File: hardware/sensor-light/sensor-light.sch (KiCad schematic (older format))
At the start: 15 parts, among them J1 Power IN 12V, J2 PIR Sensor 2, J3 PIR Sensor 1, J4 PROG Header, J5 Light Sensor, J6 PWM Power OUT 12V, Q1 IRLML2502, SW1 Manual ON/OFF, U1 Reg 3.3V, U2 MSP430G2553IN20

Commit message: Attempt at laying out the board
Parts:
- removed J1: Power IN 12V, Connectors:AK300-2, symbol CONN_01X02_MALE-RESCUE-sensor-light
- J6: value PWM Power OUT 12V -> Power IN/OUT 12V; footprint Connectors:AK300-2 -> Connectors:AK300-4; symbol CONN_01X02_FEMALE -> CONN_01X04_FEMALE-RESCUE-sensor-light
- R3: value 56 Ohm -> 47Ω
- R4: value 56 Ohm -> 27Ω
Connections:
- wire segments 44 -> 48
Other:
- moved on the sheet: C1, D1, D2, J2, J3, J4, J5, Q1, R3, R4, SW1, U1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

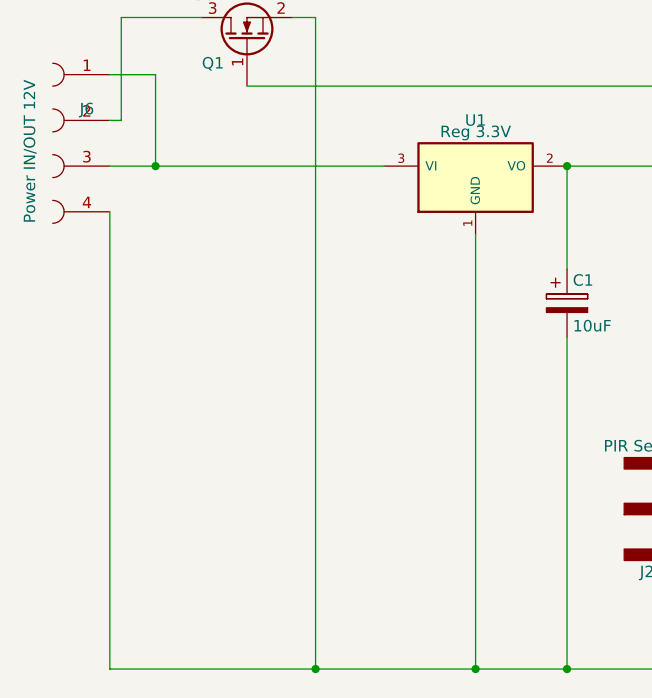
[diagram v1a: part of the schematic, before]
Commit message: add capacitor to the regulator input
Signed-off-by: Eugene Crosser <evgenii.cherkashin@profitbricks.com>
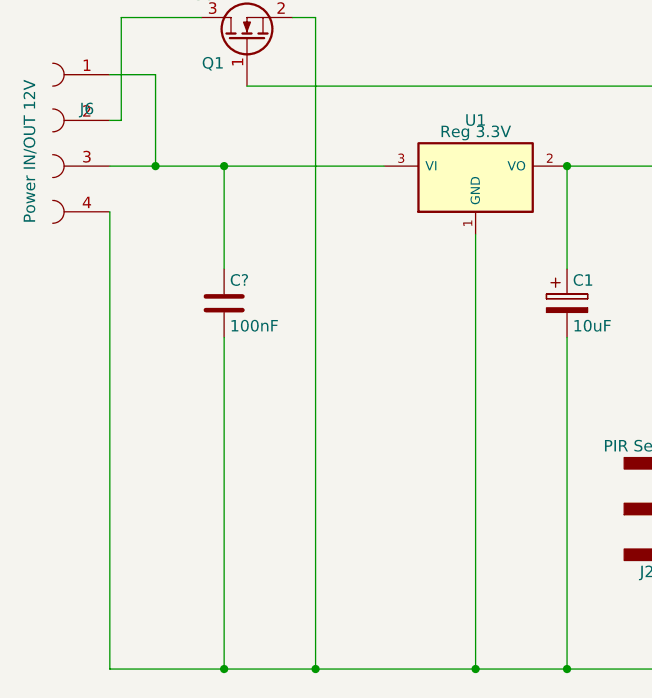
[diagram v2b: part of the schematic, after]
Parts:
- added C?: 100nF, symbol C
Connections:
- net at C1.2, D1.1 (K), D2.1 (K)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: now also C?.2
- net at J6.1, J6.3, U1.3 (VI): now also C?.1
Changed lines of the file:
@@
 Wire Wire Line
 	5300 3650 5300 4050
+$Comp
+L C C?
+U 1 1 5A8C5F51
+P 1700 3900
+F 0 "C?" H 1725 4000 50  0000 L CNN
+F 1 "100nF" H 1725 3800 50  0000 L CNN
+F 2 "" H 1738 3750 50  0000 C CNN
+F 3 "" H 1700 3900 50  0000 C CNN
+	1    1700 3900
+	1    0    0    -1
+$EndComp
+Wire Wire Line
+	1700 3750 1700 3300
+Connection ~ 1700 3300
+Wire Wire Line
+	1700 4050 1700 5500
+Connection ~ 1700 5500
 $EndSCHEMATC

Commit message: layout adjustments
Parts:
- C2: renamed from C?; footprint (none) -> Capacitors_THT:C_Rect_L7.0mm_W2.5mm_P5.00mm
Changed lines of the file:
@@
 	5300 3650 5300 4050
 $Comp
-L C C?
+L C C2
 U 1 1 5A8C5F51
 P 1700 3900
-F 0 "C?" H 1725 4000 50  0000 L CNN
+F 0 "C2" H 1725 4000 50  0000 L CNN
 F 1 "100nF" H 1725 3800 50  0000 L CNN
-F 2 "" H 1738 3750 50  0000 C CNN
+F 2 "Capacitors_THT:C_Rect_L7.0mm_W2.5mm_P5.00mm" H 1738 3750 50  0001 C CNN
 F 3 "" H 1700 3900 50  0000 C CNN
 	1    1700 3900

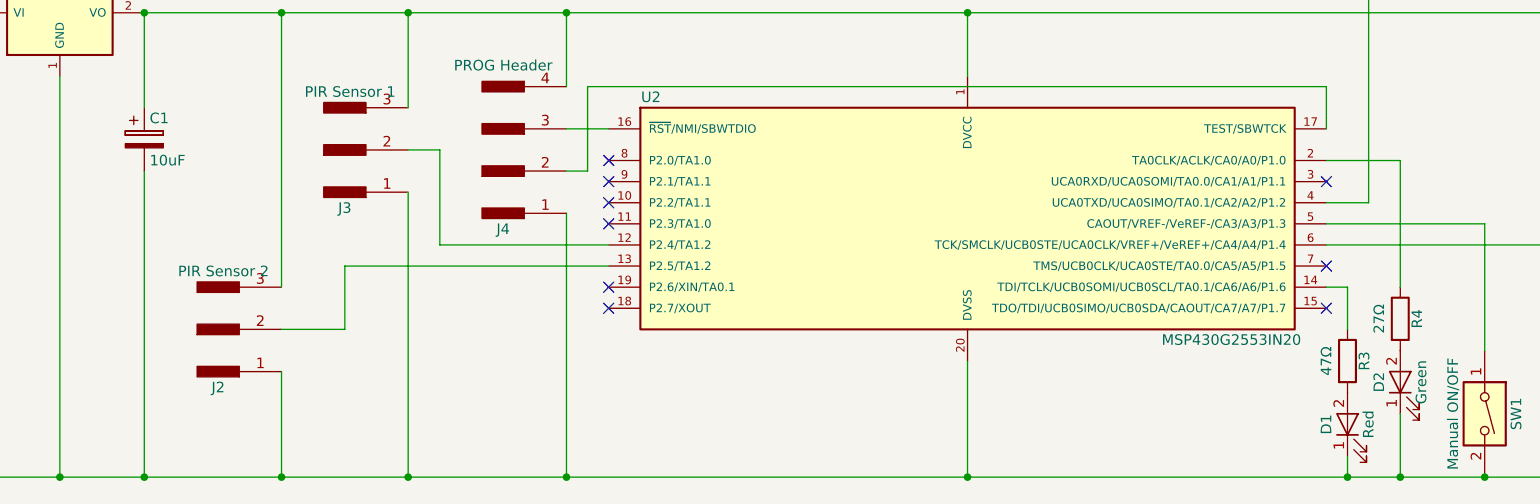
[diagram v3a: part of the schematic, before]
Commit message: minor adjustment in traces and labels
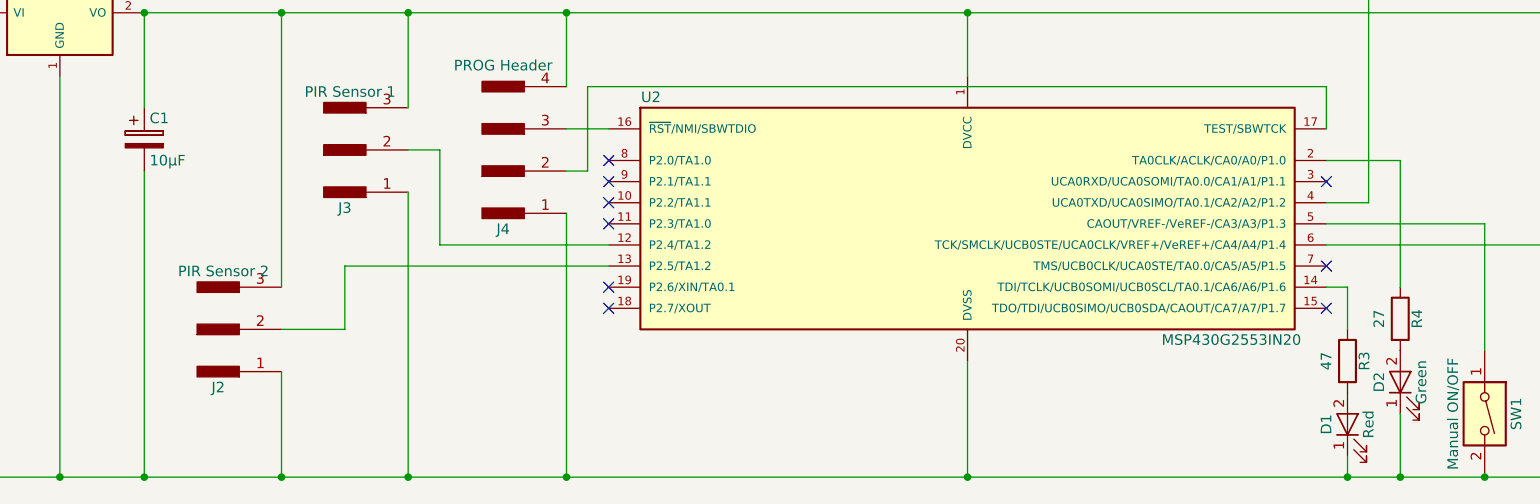
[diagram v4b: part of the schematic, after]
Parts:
- C1: value 10uF -> 10μF
- R3: value 47Ω -> 47
- R4: value 27Ω -> 27
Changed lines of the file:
@@
 P 3200 3900
 F 0 "C1" H 3225 4000 50  0000 L CNN
-F 1 "10uF" H 3225 3800 50  0000 L CNN
+F 1 "10μF" H 3225 3800 50  0000 L CNN
 F 2 "Capacitors_THT:CP_Radial_D5.0mm_P2.50mm" H 3238 3750 50  0001 C CNN
 F 3 "" H 3200 3900 50  0001 C CNN
@@
 P 8900 4950
 F 0 "R3" V 8980 4950 50  0000 C CNN
-F 1 "47Ω" V 8800 4950 50  0000 C CNN
+F 1 "47" V 8800 4950 50  0000 C CNN
 F 2 "Resistors_THT:R_Axial_DIN0411_L9.9mm_D3.6mm_P12.70mm_Horizontal" V 8830 4950 50  0001 C CNN
 F 3 "" H 8900 4950 50  0001 C CNN
@@
 P 9150 4750
 F 0 "R4" V 9230 4750 50  0000 C CNN
-F 1 "27Ω" V 9050 4750 50  0000 C CNN
+F 1 "27" V 9050 4750 50  0000 C CNN
 F 2 "Resistors_THT:R_Axial_DIN0411_L9.9mm_D3.6mm_P12.70mm_Horizontal" V 9080 4750 50  0001 C CNN
 F 3 "" H 9150 4750 50  0001 C CNN

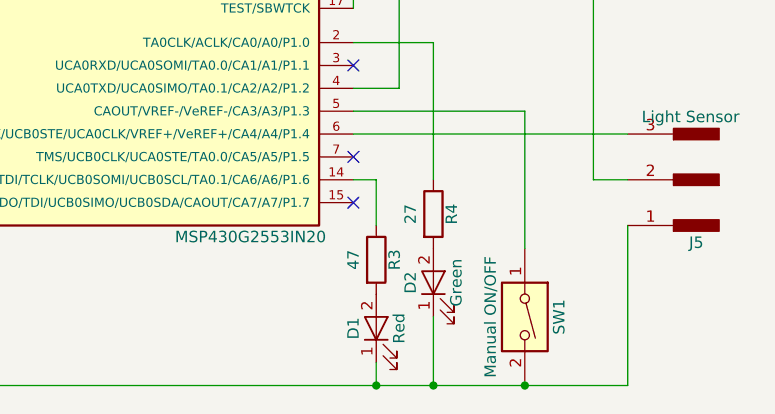
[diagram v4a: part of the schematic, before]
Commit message: Change the power connector type
because I could not order AK300 :-\

Signed-off-by: Eugene Crosser <evgenii.cherkashin@profitbricks.com>
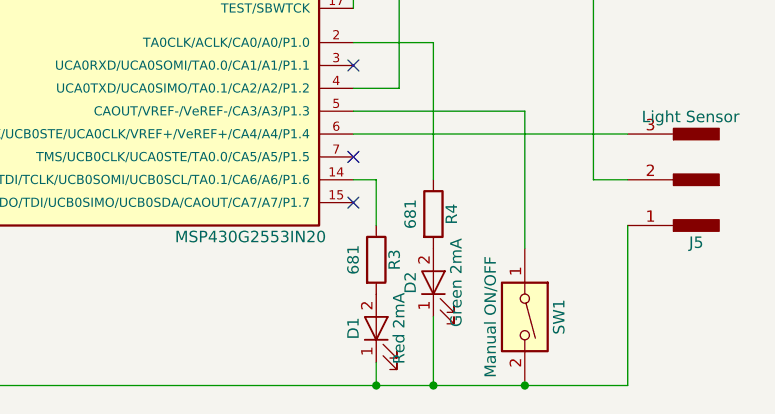
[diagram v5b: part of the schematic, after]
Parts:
- D1: value Red -> Red 2mA
- D2: value Green -> Green 2mA
- J6: footprint Connectors:AK300-4 -> local:AKZ692_4
- R3: value 47 -> 681
- R4: value 27 -> 681
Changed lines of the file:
@@
 P 9150 5050
 F 0 "D2" H 9150 5150 50  0000 C CNN
-F 1 "Green" H 9150 4950 50  0000 C CNN
+F 1 "Green 2mA" H 9150 4950 50  0000 C CNN
 F 2 "LEDs:LED_D3.0mm" H 9150 5050 50  0001 C CNN
 F 3 "" H 9150 5050 50  0001 C CNN
@@
 P 8900 5250
 F 0 "D1" H 8900 5350 50  0000 C CNN
-F 1 "Red" H 8900 5150 50  0000 C CNN
+F 1 "Red 2mA" H 8900 5150 50  0000 C CNN
 F 2 "LEDs:LED_D3.0mm" H 8900 5250 50  0001 C CNN
 F 3 "" H 8900 5250 50  0001 C CNN
@@
 P 8900 4950
 F 0 "R3" V 8980 4950 50  0000 C CNN
-F 1 "47" V 8800 4950 50  0000 C CNN
+F 1 "681" V 8800 4950 50  0000 C CNN
 F 2 "Resistors_THT:R_Axial_DIN0411_L9.9mm_D3.6mm_P12.70mm_Horizontal" V 8830 4950 50  0001 C CNN
 F 3 "" H 8900 4950 50  0001 C CNN
@@
 P 9150 4750
 F 0 "R4" V 9230 4750 50  0000 C CNN
-F 1 "27" V 9050 4750 50  0000 C CNN
+F 1 "681" V 9050 4750 50  0000 C CNN
 F 2 "Resistors_THT:R_Axial_DIN0411_L9.9mm_D3.6mm_P12.70mm_Horizontal" V 9080 4750 50  0001 C CNN
 F 3 "" H 9150 4750 50  0001 C CNN
@@
 F 0 "J6" H 1100 3350 50  0000 C CNN
 F 1 "Power IN/OUT 12V" V 1350 2850 50  0000 L CNN
-F 2 "Connectors:AK300-4" H 1100 3200 50  0001 C CNN
+F 2 "local:AKZ692_4" H 1100 3200 50  0001 C CNN
 F 3 "" H 1100 3200 50  0001 C CNN
 	1    1100 3200
